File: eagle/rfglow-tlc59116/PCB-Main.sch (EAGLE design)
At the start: 14 parts, among them IC1 TLC59116PW, J1 4P-SMD-2.0-90D, J2 2P-2.0-90D-SMD, SW1 MK-12C02 G1.5, SW2 DHT-4235A, X1 87438-06

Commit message: CLeaned up gerbers, fixed serious circuit errors
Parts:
- added C1: 100nf, Seeed-Capacitor:CERAMIC-100NF-25V-10%-X7R(0402)
- added R6, R7: 4.7K, Seeed-Resistor:SMD-RES-4.7K-5%-1/16W(0402)
- added R8, R9: 10M 1/16W, Seeed-Resistor:SMD-RES-10M-1%-1/16W(0402)
- R5: value 10K -> 10K 1/16W; device Seeed-Resistor:SMD-RES-10K-1%-1/10W(0603) -> Seeed-Resistor:SMD-RES-10K-1%-1/16W(0402)
- X1: device con-molex:87438-06 -> Components:87438-06
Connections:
- removed net N$12: IC1.SCL, U$1.18-D4/A5-SCL
- removed net N$13: IC1.SDA, U$1.19-D3/A4-SDA
- removed net N$8: MOD3.3V.VOUT, R5.1, U$1.13-VCC, X1-3.S
- new net I2CSCL: IC1.SCL, R7.1, U$1.18-D4/A5-SCL
- new net I2CSDA: IC1.SDA, R6.1, U$1.19-D3/A4-SDA
- new net V3.3: IC1.VCC, MOD3.3V.VOUT, R5.1, R6.2, R7.2, U$1.13-VCC, X1-3.S
- net GND: now also C1.1, R9.1
- net N$11: now also U$1.27-D18(PWM)-INT1; no longer U$1.26-D19-PD4
- net N$17: now also C1.2, R8.1, R9.2; no longer IC1.VCC, U$1.9-D9/A1-PC1
- net N$5: now also R8.2

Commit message: Updates to board
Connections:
- new net N$8: U$1.11-AREF, X1-2.S
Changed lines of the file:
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@@
 <?xml version="1.0" encoding="utf-8"?>
 <!DOCTYPE eagle SYSTEM "eagle.dtd">
-<eagle version="8.3.0">
+<eagle version="8.3.1">
 <drawing>
 <settings>
@@
 </segment>
 </net>
+<net name="N$8" class="0">
+<segment>
+<pinref part="U$1" gate="G$1" pin="11-AREF"/>
+<wire x1="33.02" y1="5.08" x2="33.02" y2="-7.62" width="0.1524" layer="91"/>
+<wire x1="33.02" y1="-7.62" x2="53.34" y2="-7.62" width="0.1524" layer="91"/>
+<wire x1="53.34" y1="-7.62" x2="53.34" y2="15.24" width="0.1524" layer="91"/>
+<pinref part="X1" gate="-2" pin="S"/>
+<wire x1="53.34" y1="15.24" x2="63.5" y2="15.24" width="0.1524" layer="91"/>
+</segment>
+</net>

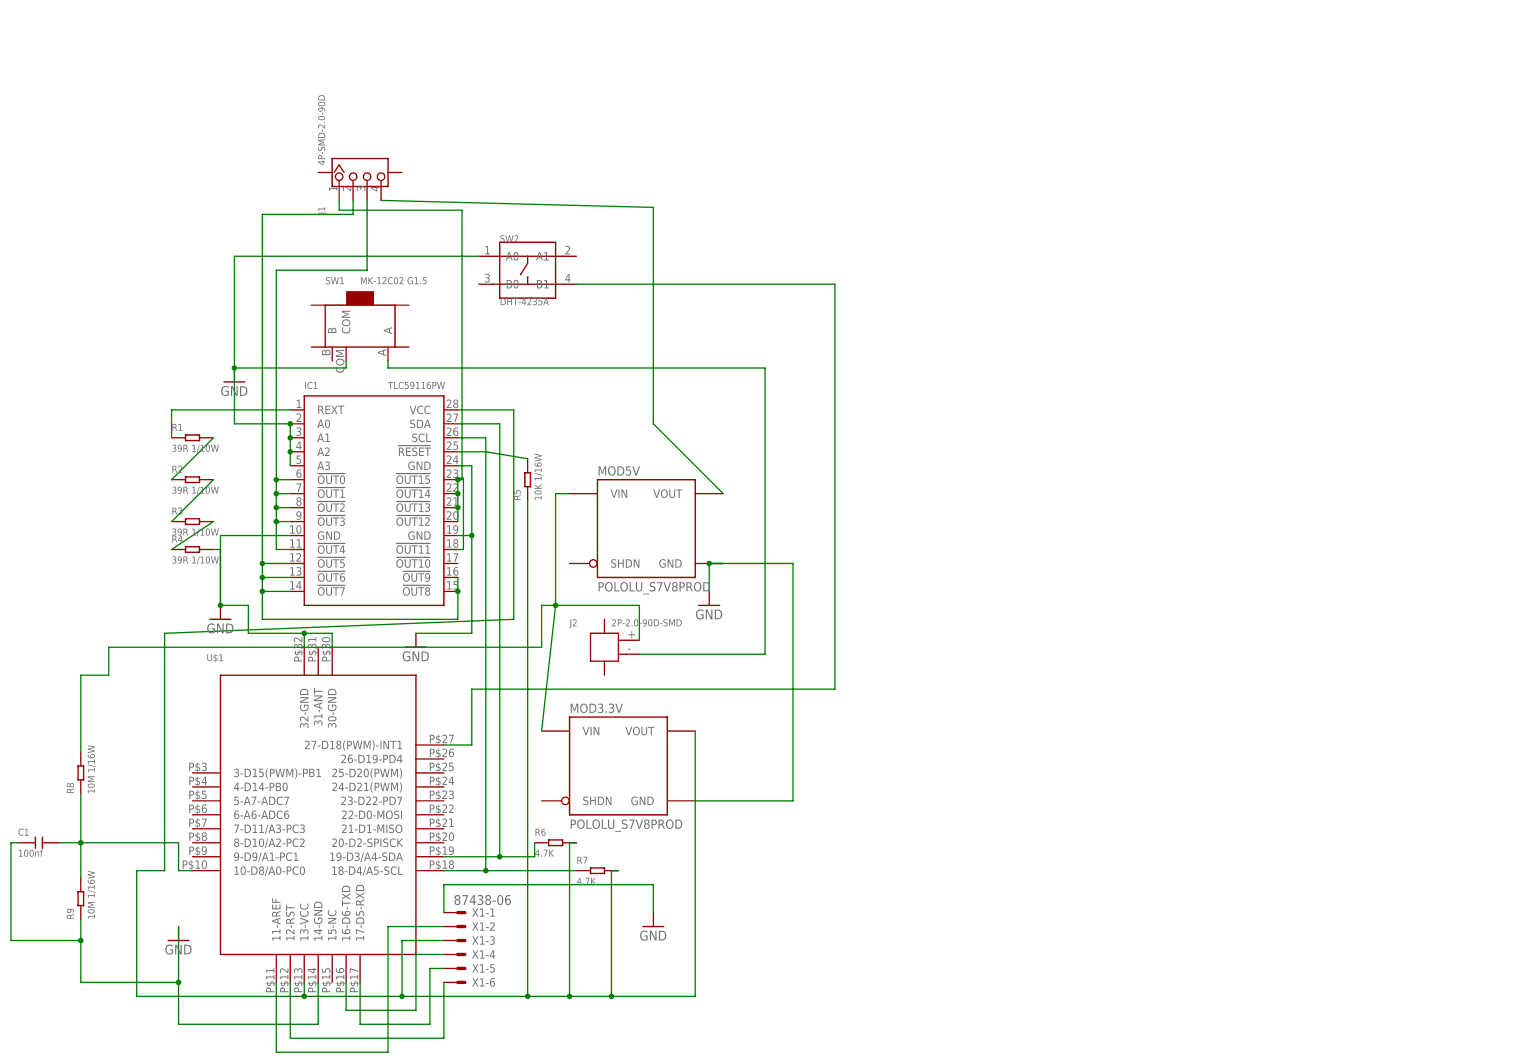
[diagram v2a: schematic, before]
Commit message: Real PCB for relay board, update handle to reduce submodules and use a u.FL antenna connector.
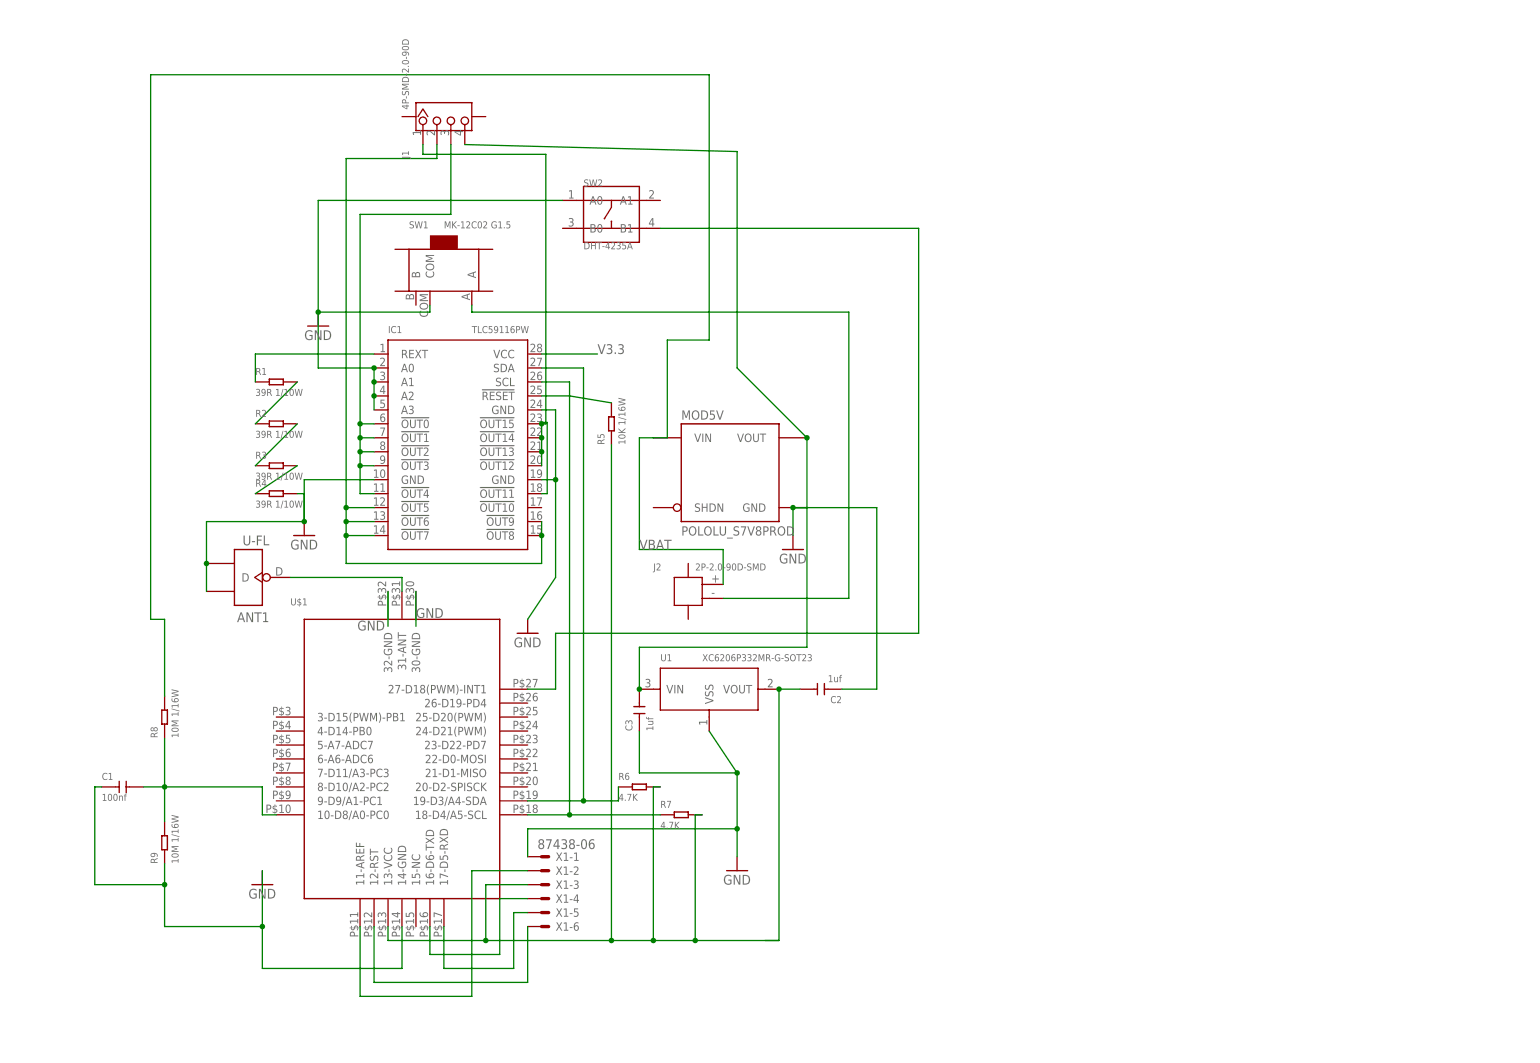
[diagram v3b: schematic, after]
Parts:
- removed MOD3.3V: POLOLU_S7V8PROD, Components:POLOLU_S7V8PROD
- added ANT1: U-FL, Seeed-Connector:ANTENNA-CONN-U-FL(3P)
- added C2, C3: 1uf, Seeed-Capacitor:CERAMIC-1UF-10V-10%-X5R(0402)
- added U1: XC6206P332MR-G-SOT23, Seeed-IC:PMIC-LDO-XC6206P332MR-G(SOT23)
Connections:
- net N$6 renamed SW-GND
- removed net N$5: J2.1, MOD3.3V.VIN, MOD5V.VIN, R8.2
- new net V4.5: C3.2, J1.4, MOD5V.VOUT, U1.VIN
- new net VBAT: J2.1, MOD5V.VIN, R8.2
- net GND: now also ANT1.GND1, ANT1.GND2, C2.1, C3.1, U1.VSS; no longer MOD3.3V.GND
- net N$1: now also ANT1.D, U$1.31-ANT; no longer J1.4, MOD5V.VOUT
- net V3.3: now also C2.2, U1.VOUT; no longer MOD3.3V.VOUT
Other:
- moved on the sheet: C1, IC1, J1, J2, MOD5V, R1, R2, R3, R4, R5, R6, R7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

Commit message: Clean up schematic
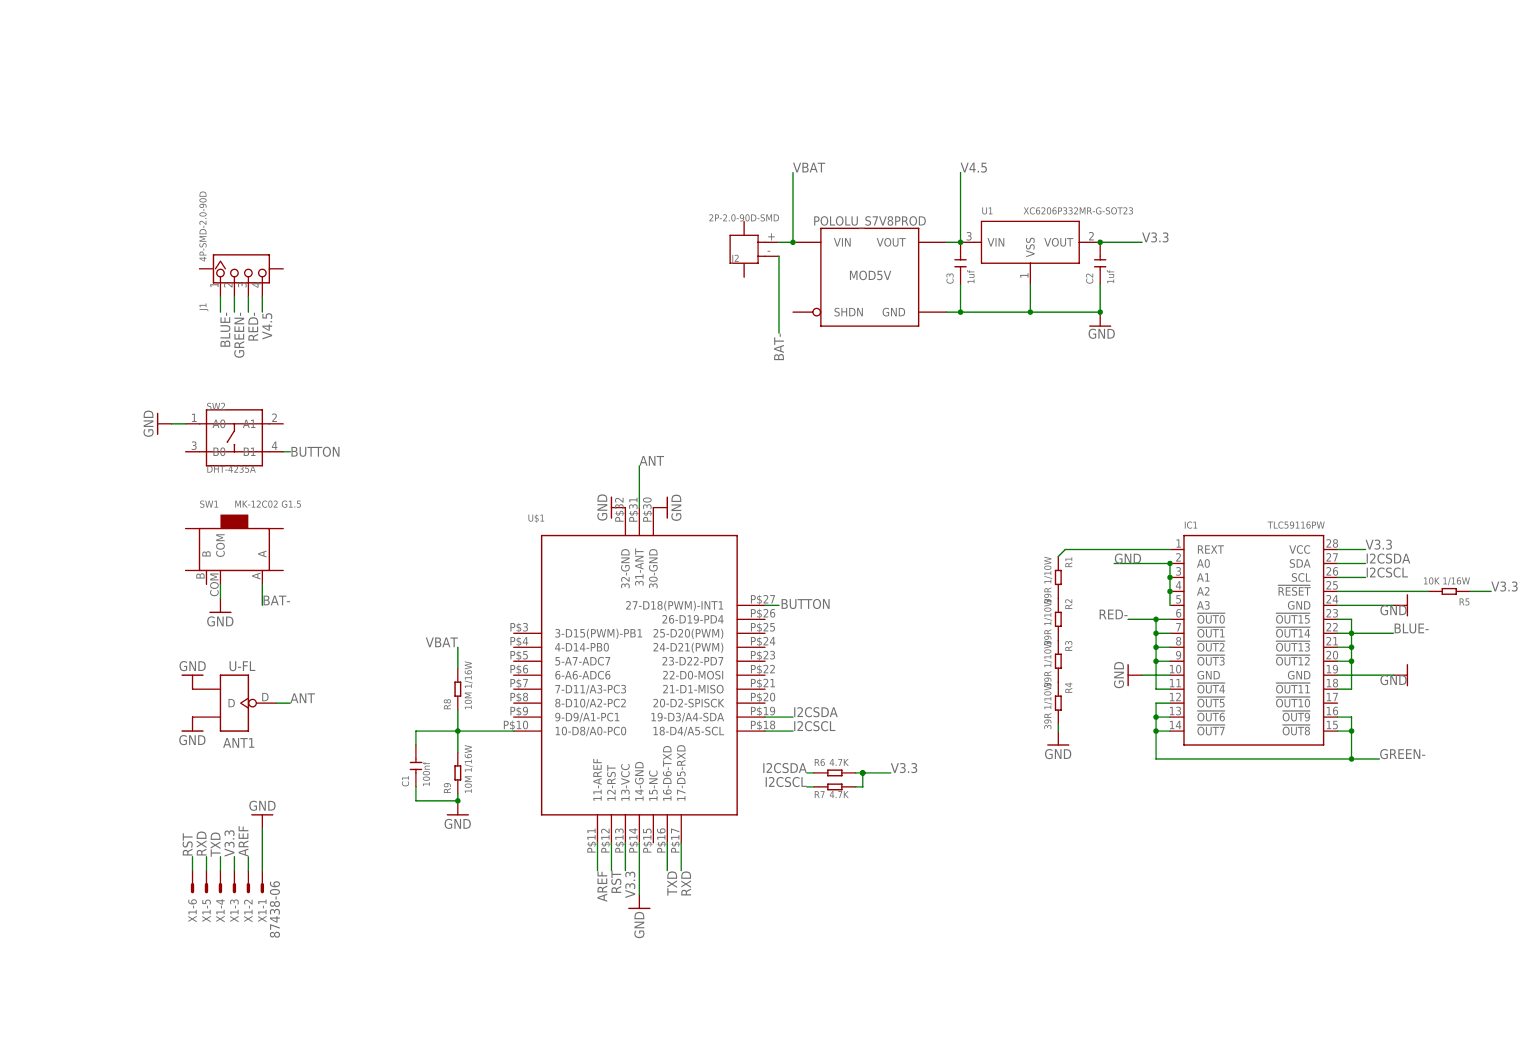
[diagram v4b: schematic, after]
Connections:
- net N$1 renamed ANT
- net N$10 renamed GREEN-
- net N$11 renamed BUTTON
- net N$14 renamed RED-
- net N$15 renamed BLUE-
- net N$16 renamed TXD
- net N$18 renamed RXD
- net N$19 renamed RST
- net N$8 renamed AREF
- net SW-GND renamed BAT-
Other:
- moved on the sheet: ANT1, C1, C2, C3, IC1, J1, J2, MOD5V, R1, R2, R3, R4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
